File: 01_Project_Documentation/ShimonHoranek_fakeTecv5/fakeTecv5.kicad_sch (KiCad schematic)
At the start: 30 parts, among them J1 Nice!nano - left pins, J10 Battery Holes, J14 GPS Pins, J2 Nice!nano - right pins, J3 Lora - left pins, J4 Lora - right pins, J5 I2C Oled screen, J6 T1 Drain - SMD, J7 T2 Drain - SMD, J8 T3 Drain - SMD, J9 Battery Connector JST 1.25, SW1 Reset, SW2 SW_Push, T1 SI2312, T2 SI2312, T3 SI2312, U1 XB8089D0

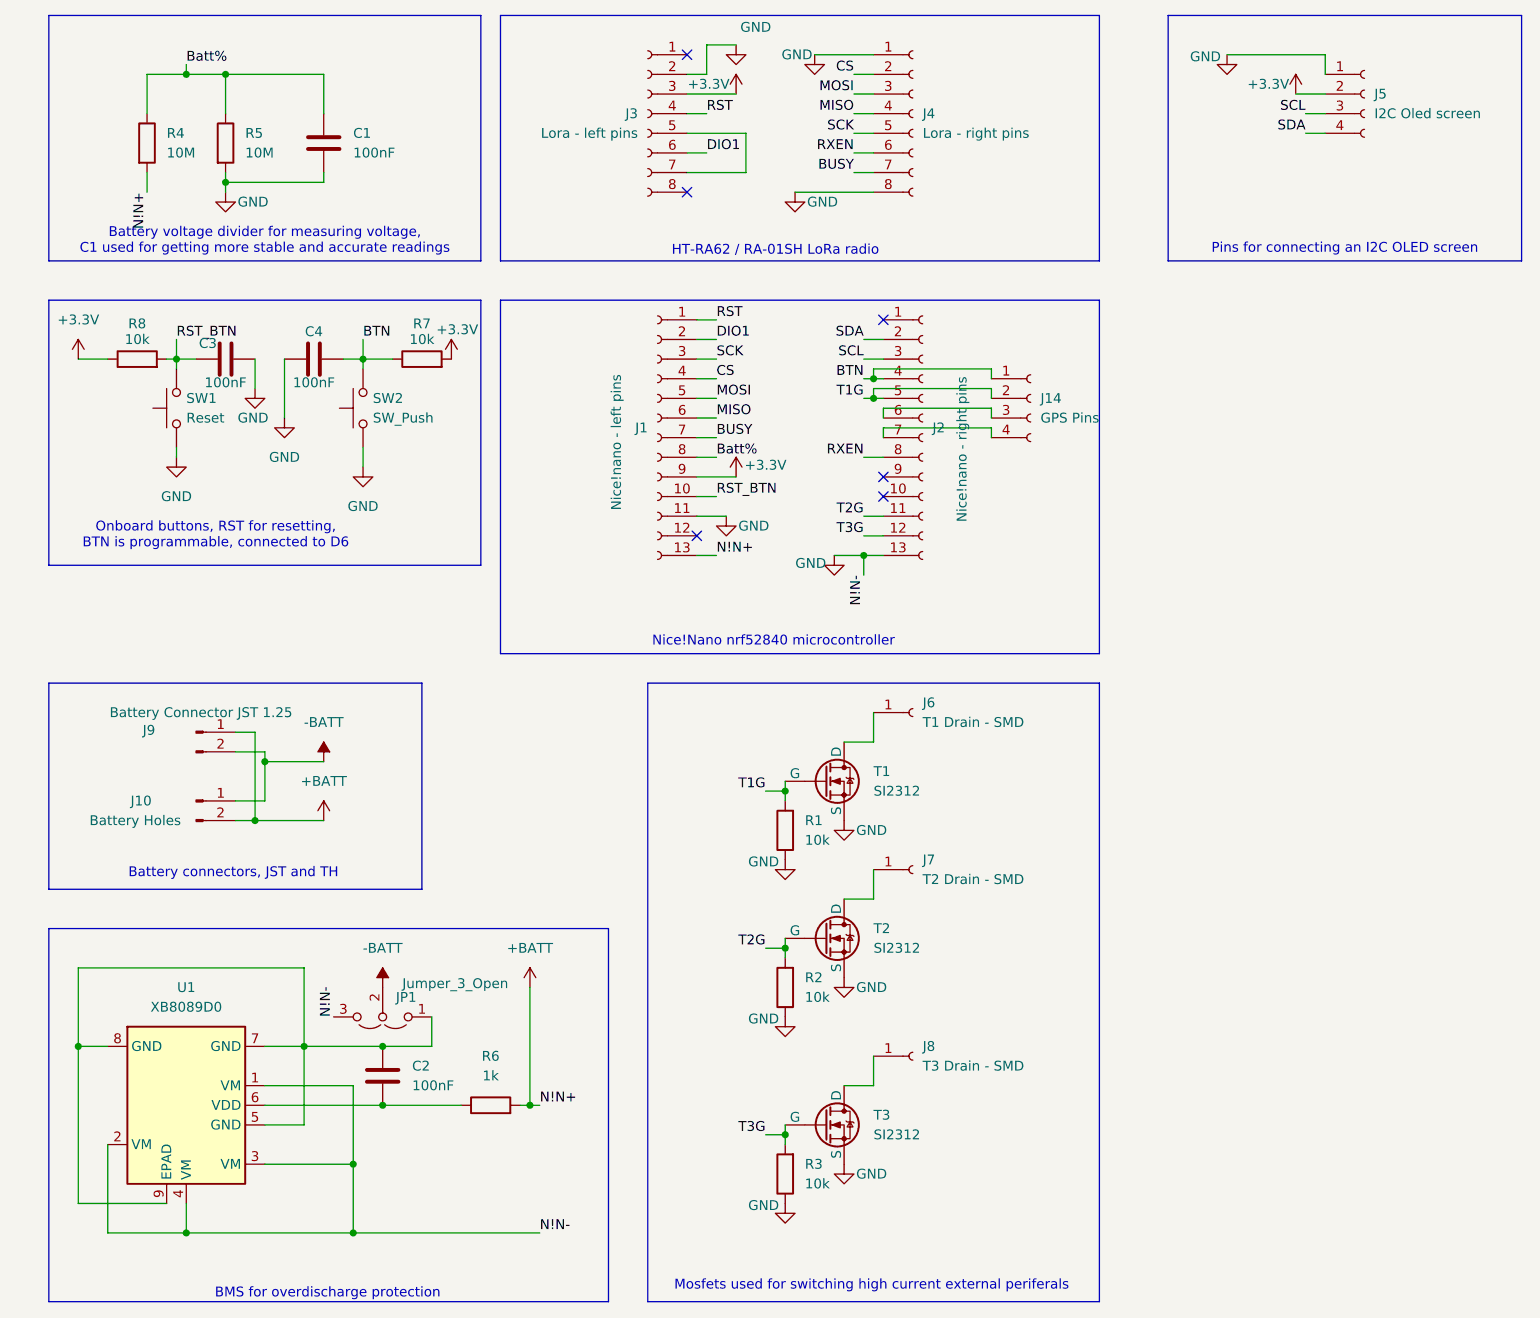
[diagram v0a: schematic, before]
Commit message: Battery protection and measure schematics
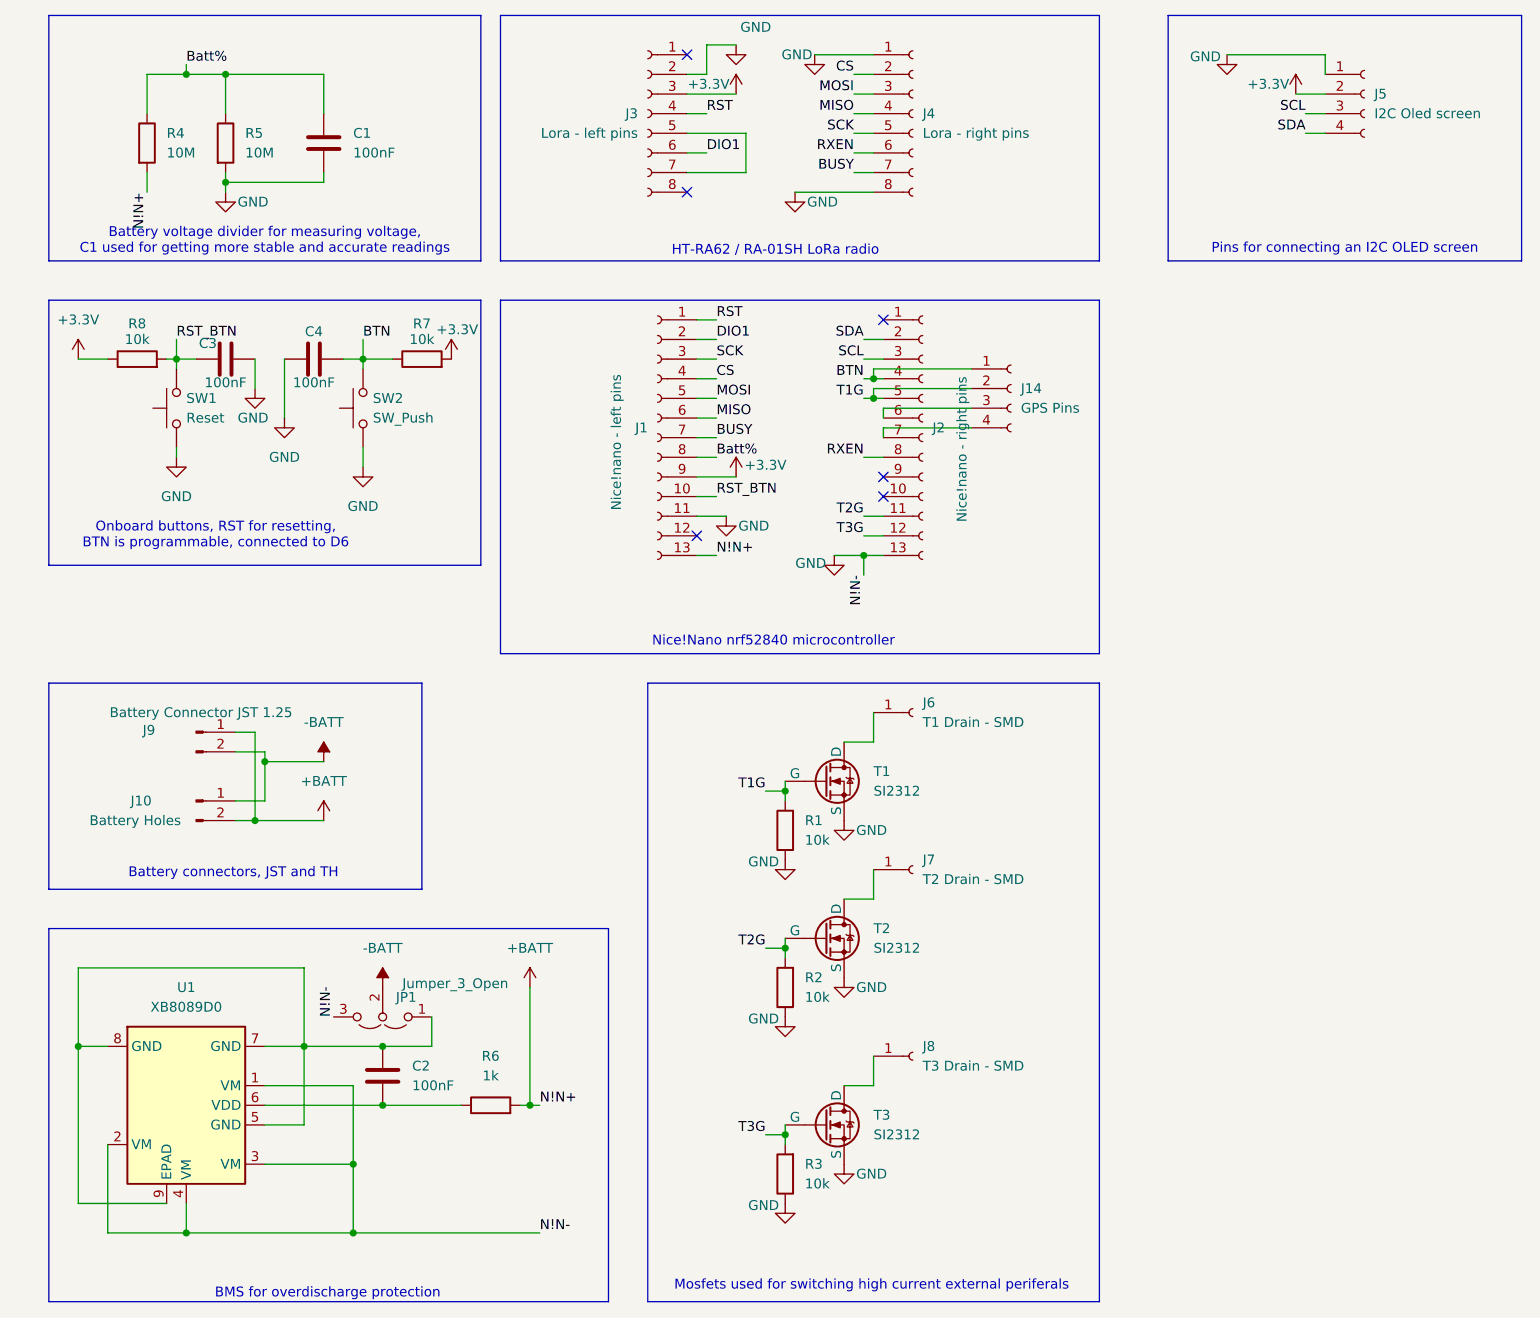
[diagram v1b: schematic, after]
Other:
- moved on the sheet: J14
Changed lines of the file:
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@@
 (kicad_sch
-	(version 20231120)
+	(version 20250114)
 	(generator "eeschema")
-	(generator_version "8.0")
+	(generator_version "9.0")
 	(paper "A4")
 	(title_block
@@
 		(rev "2")
 	)
+	(rectangle
+		(start 19.05 17.78)
+		(end 74.93 49.53)
+		(stroke
+			(width 0)
+			(type default)
+		)
+		(fill
+			(type none)
+		)
+	)
+	(rectangle
+		(start 163.83 17.78)
+		(end 209.55 49.53)
+		(stroke
+			(width 0)
+			(type default)
+		)
+		(fill
+			(type none)
+		)
+	)
+	(rectangle
+		(start 77.47 17.78)
+		(end 154.94 49.53)
+		(stroke
+			(width 0)
+			(type default)
+		)
+		(fill
+			(type none)
+		)
+	)
+	(rectangle
+		(start 19.05 54.61)
+		(end 74.93 88.9)
+		(stroke
+			(width 0)
+			(type default)
+		)
+		(fill
+			(type none)
+		)
+	)
+	(rectangle
+		(start 96.52 104.14)
+		(end 154.94 184.15)
+		(stroke
+			(width 0)
+			(type default)
+		)
+		(fill
+			(type none)
+		)
+	)
+	(rectangle
+		(start 19.05 104.14)
+		(end 67.31 130.81)
+		(stroke
+			(width 0)
+			(type default)
+		)
+		(fill
+			(type none)
+		)
+	)
+	(rectangle
+		(start 77.47 54.61)
+		(end 154.94 100.33)
+		(stroke
+			(width 0)
+			(type default)
+		)
+		(fill
+			(type none)
+		)
+	)
+	(rectangle
+		(start 19.05 135.89)
+		(end 91.44 184.15)
+		(stroke
+			(width 0)
+			(type default)
+		)
+		(fill
+			(type none)
+		)
+	)
+	(text "Nice!Nano nrf52840 microcontroller\n"
+		(exclude_from_sim no)
+		(at 112.776 98.806 0)
+		(effects
+			(font
+				(size 1.27 1.27)
+			)
+		)
+	)
+	(text "Mosfets used for switching high current external periferals"
+		(exclude_from_sim no)
+		(at 125.476 182.118 0)
+		(effects
+			(font
+				(size 1.27 1.27)
+			)
+		)
+	)
+	(text "BMS for overdischarge protection"
+		(exclude_from_sim no)
+		(at 55.118 183.134 0)
+		(effects
+			(font
+				(size 1.27 1.27)
+			)
+		)
+	)
+	(text "Battery voltage divider for measuring voltage,\nC1 used for getting more stable and accurate readings"
+		(exclude_from_sim no)
+		(at 46.99 46.99 0)
+		(effects
+			(font
+				(size 1.27 1.27)
+			)
+		)
+	)
+	(text "HT-RA62 / RA-01SH LoRa radio"
+		(exclude_from_sim no)
+		(at 113.03 48.26 0)
+		(effects
+			(font
+				(size 1.27 1.27)
+			)
+		)
+	)
+	(text "Onboard buttons, RST for resetting,\nBTN is programmable, connected to D6\n\n"
+		(exclude_from_sim no)
+		(at 40.64 86.106 0)
+		(effects
+			(font
+				(size 1.27 1.27)
+			)
+		)
+	)
+	(text "Battery connectors, JST and TH\n\n"
+		(exclude_from_sim no)
+		(at 42.926 129.794 0)
+		(effects
+			(font
+				(size 1.27 1.27)
+			)
+		)
+	)
+	(text "Pins for connecting an I2C OLED screen\n"
+		(exclude_from_sim no)
+		(at 186.69 48.006 0)
+		(effects
+			(font
+				(size 1.27 1.27)
+			)
+		)
+	)
 	(junction
 		(at 59.69 62.23)
@@
 	(wire
 		(pts
-			(xy 127 68.58) (xy 140.97 68.58)
-		)
-		(stroke
-			(width 0)
-			(type default)
-		)
-	)
-	(wire
-		(pts
-			(xy 140.97 68.58) (xy 140.97 69.85)
+			(xy 127 68.58) (xy 138.43 68.58)
 		)
 		(stroke
@@
 	(wire
 		(pts
-			(xy 125.73 63.5) (xy 140.97 63.5)
+			(xy 125.73 63.5) (xy 138.43 63.5)
 		)
 		(stroke
@@
 	(wire
 		(pts
-			(xy 127 71.12) (xy 140.97 71.12)
+			(xy 127 71.12) (xy 138.43 71.12)
 		)
 		(stroke
@@
 	(wire
 		(pts
-			(xy 140.97 71.12) (xy 140.97 72.39)
-		)
-		(stroke
-			(width 0)
-			(type default)
-		)
-	)
-	(wire
-		(pts
 			(xy 26.67 163.83) (xy 26.67 175.26)
 		)
@@
 	(wire
 		(pts
-			(xy 140.97 63.5) (xy 140.97 64.77)
-		)
-		(stroke
-			(width 0)
-			(type default)
-		)
-	)
-	(wire
-		(pts
 			(xy 114.3 137.16) (xy 114.3 138.43)
 		)
@@
 	(wire
 		(pts
-			(xy 140.97 66.04) (xy 140.97 67.31)
-		)
-		(stroke
-			(width 0)
-			(type default)
-		)
-	)
-	(wire
-		(pts
 			(xy 52.07 140.97) (xy 52.07 151.13)
 		)
@@
 	(wire
 		(pts
-			(xy 125.73 66.04) (xy 140.97 66.04)
-		)
-		(stroke
-			(width 0)
-			(type default)
-		)
-	)
-	(rectangle
-		(start 19.05 17.78)
-		(end 74.93 49.53)
-		(stroke
-			(width 0)
-			(type default)
-		)
-		(fill
-			(type none)
-		)
-	)
-	(rectangle
-		(start 163.83 17.78)
-		(end 209.55 49.53)
-		(stroke
-			(width 0)
-			(type default)
-		)
-		(fill
-			(type none)
-		)
-	)
-	(rectangle
-		(start 77.47 17.78)
-		(end 154.94 49.53)
-		(stroke
-			(width 0)
-			(type default)
-		)
-		(fill
-			(type none)
-		)
-	)
-	(rectangle
-		(start 19.05 54.61)
-		(end 74.93 88.9)
-		(stroke
-			(width 0)
-			(type default)
-		)
-		(fill
-			(type none)
-		)
-	)
-	(rectangle
-		(start 96.52 104.14)
-		(end 154.94 184.15)
-		(stroke
-			(width 0)
-			(type default)
-		)
-		(fill
-			(type none)
-		)
-	)
-	(rectangle
-		(start 19.05 104.14)
-		(end 67.31 130.81)
-		(stroke
-			(width 0)
-			(type default)
-		)
-		(fill
-			(type none)
-		)
-	)
-	(rectangle
-		(start 77.47 54.61)
-		(end 154.94 100.33)
-		(stroke
-			(width 0)
-			(type default)
+			(xy 125.73 66.04) (xy 138.43 66.04)
 		)
-		(fill
-			(type none)
-		)
-	)
-	(rectangle
-		(start 19.05 135.89)
-		(end 91.44 184.15)
 		(stroke
 			(width 0)
 			(type default)
 		)
-		(fill
-			(type none)
-		)
-	)
-	(text "Nice!Nano nrf52840 microcontroller\n"
-		(exclude_from_sim no)
-		(at 112.776 98.806 0)
-		(effects
-			(font
-				(size 1.27 1.27)
-			)
-		)
-	)
-	(text "Mosfets used for switching high current external periferals"
-		(exclude_from_sim no)
-		(at 125.476 182.118 0)
-		(effects
-			(font
-				(size 1.27 1.27)
-			)
-		)
-	)
-	(text "BMS for overdischarge protection"
-		(exclude_from_sim no)
-		(at 55.118 183.134 0)
-		(effects
-			(font
-				(size 1.27 1.27)
-			)
-		)
-	)
-	(text "Battery voltage divider for measuring voltage,\nC1 used for getting more stable and accurate readings"
-		(exclude_from_sim no)
-		(at 46.99 46.99 0)
-		(effects
-			(font
-				(size 1.27 1.27)
-			)
-		)
-	)
-	(text "HT-RA62 / RA-01SH LoRa radio"
-		(exclude_from_sim no)
-		(at 113.03 48.26 0)
-		(effects
-			(font
-				(size 1.27 1.27)
-			)
-		)
-	)
-	(text "Onboard buttons, RST for resetting,\nBTN is programmable, connected to D6\n\n"
-		(exclude_from_sim no)
-		(at 40.64 86.106 0)
-		(effects
-			(font
-				(size 1.27 1.27)
-			)
-		)
-	)
-	(text "Battery connectors, JST and TH\n\n"
-		(exclude_from_sim no)
-		(at 42.926 129.794 0)
-		(effects
-			(font
-				(size 1.27 1.27)
-			)
-		)
-	)
-	(text "Pins for connecting an I2C OLED screen\n"
-		(exclude_from_sim no)
-		(at 186.69 48.006 0)
-		(effects
-			(font
-				(size 1.27 1.27)
-			)
-		)
 	)
 	(label "RST_BTN"
@@
 	(symbol
 		(lib_id "Connector:Conn_01x04_Socket")
-		(at 146.05 67.31 0)
+		(at 143.51 66.04 0)
 		(unit 1)
 		(exclude_from_sim no)
@@
 		(fields_autoplaced yes)
 		(property "Reference" "J14"
-			(at 147.32 67.3099 0)
+			(at 144.78 66.0399 0)
 			(effects
 				(font
@@
 		)
 		(property "Value" "GPS Pins"
-			(at 147.32 69.8499 0)
+			(at 144.78 68.5799 0)
 			(effects
 				(font
@@
 		)
 		(property "Footprint" "SMD_PAD:SMD_PAD_4x1"
-			(at 146.05 67.31 0)
+			(at 143.51 66.04 0)
 			(effects
 				(font
@@
 		)
 		(property "Datasheet" "~"
-			(at 146.05 67.31 0)
+			(at 143.51 66.04 0)
 			(effects
 				(font
@@
 		)
 		(property "Description" "Generic connector, single row, 01x04, script generated"
-			(at 146.05 67.31 0)
+			(at 143.51 66.04 0)
 			(effects
 				(font
@@
 		)
 	)
+	(embedded_fonts no)
 )
